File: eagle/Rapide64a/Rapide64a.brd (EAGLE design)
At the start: 50 x 50 mm, 25 parts, among them IC1 MEGA64-A, J1 AVR_SPI_PRG_6PTH

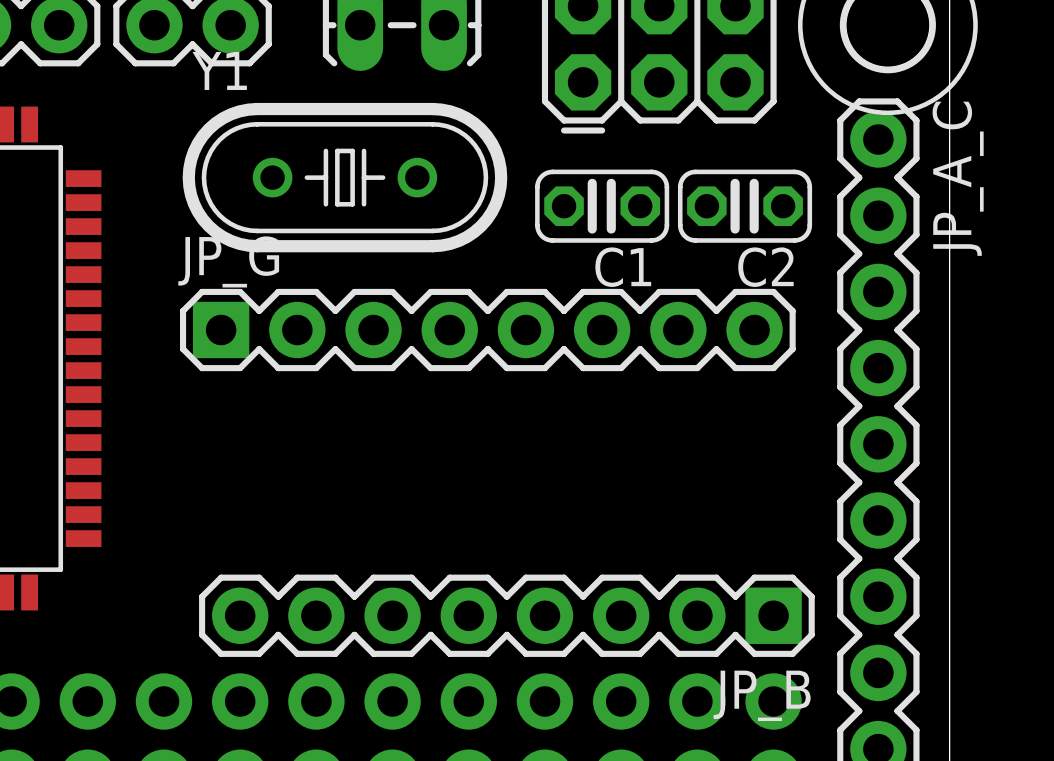
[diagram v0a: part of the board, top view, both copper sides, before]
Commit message: Added 2 pushbuttons
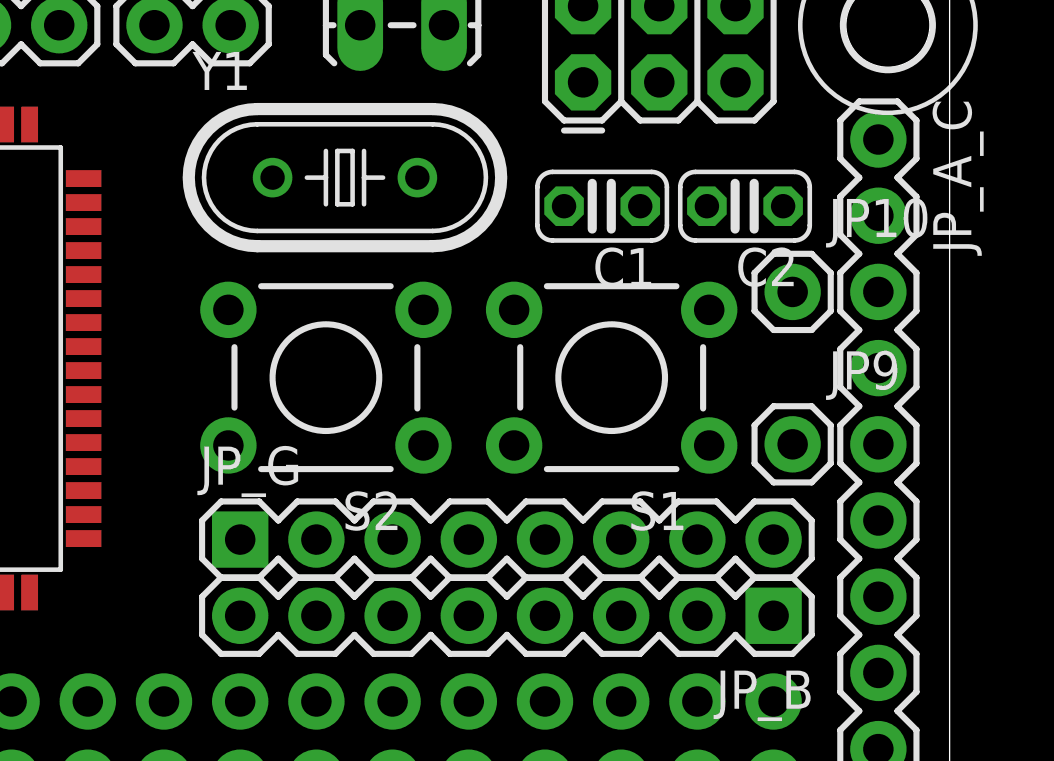
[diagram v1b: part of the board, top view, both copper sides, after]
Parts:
- added JP10, JP9: M01PTH, SparkFun-Connectors:1X01
- added S1, S2: SWITCH-MOMENTARY-2PTH, SparkFun-Electromechanical:TACTILE-PTH
- moved JP_G 7.01 mm to (26.4, 30.8)
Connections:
- new net N$55: JP9.1, S1.3
- new net N$56: JP10.1, S2.3
- net GND: now also S1.1, S2.1
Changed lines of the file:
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@@
 <element name="JP_B" library="SparkFun-Connectors" package="1X08" value="" x="44.1325" y="28.2575" rot="R180"/>
 <element name="JP_F" library="SparkFun-Connectors" package="1X08" value="" x="2.54" y="47.9425"/>
-<element name="JP_G" library="SparkFun-Connectors" package="1X08" value="" x="25.7175" y="37.7825"/>
+<element name="JP_G" library="SparkFun-Connectors" package="1X08" value="" x="26.3525" y="30.7975"/>
 <element name="JP_X" library="SparkFun-Connectors" package="1X02" value="" x="23.495" y="47.9425"/>
 <element name="C1" library="resistor" package="C025-024X044" value="22pF" x="38.4175" y="41.91" rot="R180"/>
@@
 <element name="H3" library="holes" package="2,8" value="MOUNT-HOLE2.8" x="47.9425" y="47.9425"/>
 <element name="JP8" library="SparkFun-Connectors" package="1X16_NO_SILK" value="M161X16_NO_SILK" x="6.0325" y="2.54"/>
+<element name="S1" library="SparkFun-Electromechanical" package="TACTILE-PTH" value="SWITCH-MOMENTARY-2PTH" x="38.735" y="36.195" rot="R180"/>
+<element name="S2" library="SparkFun-Electromechanical" package="TACTILE-PTH" value="SWITCH-MOMENTARY-2PTH" x="29.21" y="36.195" rot="R180"/>
+<element name="JP9" library="SparkFun-Connectors" package="1X01" value="M01PTH" x="44.7675" y="33.9725"/>
+<element name="JP10" library="SparkFun-Connectors" package="1X01" value="M01PTH" x="44.7675" y="39.0525"/>
 </elements>
 <signals>
@@
 <contactref element="J1" pad="3"/>
 <wire x1="41.5925" y1="28.2575" x2="40.3225" y2="46.0375" width="0" layer="19" extent="1-1"/>
-<wire x1="5.535" y1="34.83" x2="41.5925" y2="28.2575" width="0" layer="19" extent="1-1"/>
+<wire x1="5.535" y1="34.83" x2="40.3225" y2="46.0375" width="0" layer="19" extent="1-1"/>
 </signal>
 <signal name="N$35">
@@
 <contactref element="JP_G" pad="1"/>
 <contactref element="IC1" pad="1"/>
-<wire x1="5.535" y1="42.83" x2="25.7175" y2="37.7825" width="0" layer="19" extent="1-1"/>
+<wire x1="5.535" y1="42.83" x2="26.3525" y2="30.7975" width="0" layer="19" extent="1-1"/>
 </signal>
 <signal name="N$50">
 <contactref element="JP_G" pad="2"/>
 <contactref element="IC1" pad="33"/>
-<wire x1="21.135" y1="30.83" x2="28.2575" y2="37.7825" width="0" layer="19" extent="1-1"/>
+<wire x1="21.135" y1="30.83" x2="28.8925" y2="30.7975" width="0" layer="19" extent="1-1"/>
 </signal>
 <signal name="N$51">
 <contactref element="JP_G" pad="3"/>
 <contactref element="IC1" pad="34"/>
-<wire x1="21.135" y1="31.63" x2="30.7975" y2="37.7825" width="0" layer="19" extent="1-1"/>
+<wire x1="21.135" y1="31.63" x2="31.4325" y2="30.7975" width="0" layer="19" extent="1-1"/>
 </signal>
 <signal name="N$52">
 <contactref element="JP_G" pad="4"/>
 <contactref element="IC1" pad="43"/>
-<wire x1="21.135" y1="38.83" x2="33.3375" y2="37.7825" width="0" layer="19" extent="1-1"/>
+<wire x1="21.135" y1="38.83" x2="33.9725" y2="30.7975" width="0" layer="19" extent="1-1"/>
 </signal>
 <signal name="N$53">
 <contactref element="JP_G" pad="5"/>
 <contactref element="IC1" pad="19"/>
-<wire x1="8.935" y1="29.03" x2="35.8775" y2="37.7825" width="0" layer="19" extent="1-1"/>
+<wire x1="8.935" y1="29.03" x2="36.5125" y2="30.7975" width="0" layer="19" extent="1-1"/>
 </signal>
 <signal name="N$54">
 <contactref element="JP_G" pad="6"/>
 <contactref element="IC1" pad="18"/>
-<wire x1="8.135" y1="29.03" x2="38.4175" y2="37.7825" width="0" layer="19" extent="1-1"/>
+<wire x1="8.135" y1="29.03" x2="39.0525" y2="30.7975" width="0" layer="19" extent="1-1"/>
 </signal>
 <signal name="VCC">
@@
 <contactref element="JP_ROW_VCC" pad="16"/>
 <wire x1="33.147" y1="47.9425" x2="37.7825" y2="48.5775" width="0" layer="19" extent="1-1"/>
-<wire x1="43.4975" y1="37.7825" x2="37.7825" y2="48.5775" width="0" layer="19" extent="1-1"/>
 <wire x1="16.935" y1="44.63" x2="33.147" y2="47.9425" width="0" layer="19" extent="1-1"/>
 <wire x1="7.335" y1="44.63" x2="16.935" y2="44.63" width="0" layer="19" extent="1-1"/>
 <wire x1="10.535" y1="29.03" x2="7.335" y2="44.63" width="0" layer="19" extent="1-1"/>
+<wire x1="44.1325" y1="30.7975" x2="37.7825" y2="48.5775" width="0" layer="19" extent="1-1"/>
 <wire x1="11.1125" y1="10.16" x2="10.535" y2="29.03" width="0" layer="19" extent="1-1"/>
 <wire x1="13.6525" y1="10.16" x2="11.1125" y2="10.16" width="0" layer="19" extent="1-1"/>
@@
 <contactref element="JP_ROW_GND" pad="2"/>
 <contactref element="JP_ROW_GND" pad="1"/>
+<contactref element="S1" pad="1"/>
+<contactref element="S2" pad="1"/>
 <wire x1="44.45" y1="41.91" x2="42.8625" y2="48.5775" width="0" layer="19" extent="1-1"/>
-<wire x1="40.9575" y1="37.7825" x2="44.45" y2="41.91" width="0" layer="19" extent="1-1"/>
-<wire x1="39.6875" y1="41.91" x2="40.9575" y2="37.7825" width="0" layer="19" extent="1-1"/>
+<wire x1="39.6875" y1="41.91" x2="44.45" y2="41.91" width="0" layer="19" extent="1-1"/>
+<wire x1="41.9862" y1="33.9344" x2="39.6875" y2="41.91" width="0" layer="19" extent="1-1"/>
+<wire x1="41.5925" y1="30.7975" x2="41.9862" y2="33.9344" width="0" layer="19" extent="1-1"/>
+<wire x1="32.4612" y1="33.9344" x2="41.9862" y2="33.9344" width="0" layer="19" extent="1-1"/>
 <wire x1="30.353" y1="47.9425" x2="39.6875" y2="41.91" width="0" layer="19" extent="1-1"/>
 <wire x1="16.135" y1="44.63" x2="30.353" y2="47.9425" width="0" layer="19" extent="1-1"/>
 <wire x1="8.135" y1="44.63" x2="16.135" y2="44.63" width="0" layer="19" extent="1-1"/>
 <wire x1="11.335" y1="29.03" x2="8.135" y2="44.63" width="0" layer="19" extent="1-1"/>
-<wire x1="13.6525" y1="12.7" x2="11.335" y2="29.03" width="0" layer="19" extent="1-1"/>
+<wire x1="11.1125" y1="12.7" x2="11.335" y2="29.03" width="0" layer="19" extent="1-1"/>
+<wire x1="13.6525" y1="12.7" x2="11.1125" y2="12.7" width="0" layer="19" extent="1-1"/>
 <wire x1="16.1925" y1="12.7" x2="13.6525" y2="12.7" width="0" layer="19" extent="1-1"/>
 <wire x1="18.7325" y1="12.7" x2="16.1925" y2="12.7" width="0" layer="19" extent="1-1"/>
@@
 <wire x1="41.5925" y1="12.7" x2="39.0525" y2="12.7" width="0" layer="19" extent="1-1"/>
 <wire x1="44.1325" y1="12.7" x2="41.5925" y2="12.7" width="0" layer="19" extent="1-1"/>
-<wire x1="11.1125" y1="12.7" x2="13.6525" y2="12.7" width="0" layer="19" extent="1-1"/>
 <wire x1="8.5725" y1="12.7" x2="11.1125" y2="12.7" width="0" layer="19" extent="1-1"/>
 <wire x1="6.0325" y1="12.7" x2="8.5725" y2="12.7" width="0" layer="19" extent="1-1"/>
 </signal>
+<signal name="N$55">
+<contactref element="S1" pad="3"/>
+<contactref element="JP9" pad="1"/>
+<wire x1="44.7675" y1="33.9725" x2="41.9862" y2="38.4556" width="0" layer="19" extent="1-1"/>
+</signal>
+<signal name="N$56">
+<contactref element="S2" pad="3"/>
+<contactref element="JP10" pad="1"/>
+<wire x1="32.4612" y1="38.4556" x2="44.7675" y2="39.0525" width="0" layer="19" extent="1-1"/>
+</signal>
 </signals>

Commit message: Work in progress, 40% wiring done.
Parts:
- JP_POWER: device SparkFun-Connectors:1X02_LOCK_LONGPADS -> SparkFun-Connectors:1X02
- moved JP_B 17.8 mm to (26.4, 28.3), turned to 0 degrees
- moved JP_F 0.71 mm to (1.91, 48.3)
- moved JP_X 0.71 mm to (24.1, 48.3)
- moved J1 0.32 mm to (37.8, 45.7)
- moved Y1 0.32 mm to (30.2, 42.9), turned to 180 degrees
- moved JP_G 0.32 mm to (26.4, 31.1)
- moved C1 0.32 mm to (38.4, 41.6)
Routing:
- net GND: track 0.00 -> 160.1 mm, vias 0 -> 2
- net VCC: track 0.00 -> 129.0 mm, vias 0 -> 2
- net N$68: track 0.00 -> 53.1 mm
- net N$17: track 0.00 -> 50.7 mm, vias 0 -> 1
- net N$35: track 0.00 -> 47.5 mm
- net N$67: track 0.00 -> 47.0 mm
- net N$44: track 0.00 -> 46.2 mm, vias 0 -> 1
- net N$36: track 0.00 -> 42.2 mm
- net N$66: track 0.00 -> 40.4 mm
- net N$43: track 0.00 -> 39.9 mm, vias 0 -> 1
- net N$65: track 0.00 -> 34.3 mm
- net N$58: track 0.00 -> 27.5 mm, vias 0 -> 1
- net N$64: track 0.00 -> 27.1 mm
- net N$8: track 0.00 -> 22.1 mm
- net N$6: track 0.00 -> 21.4 mm, vias 0 -> 1
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
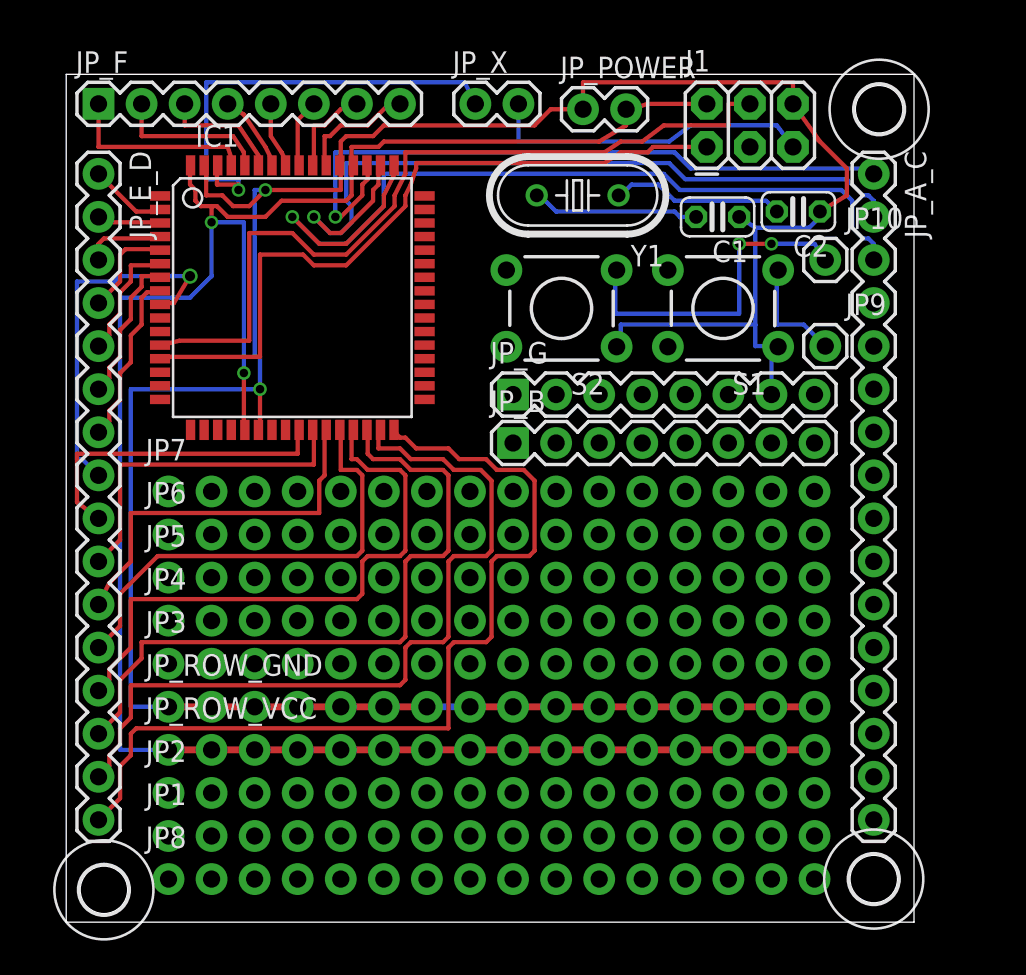
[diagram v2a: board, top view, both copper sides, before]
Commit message: Work in progress, changed layout a little, 60% wiring
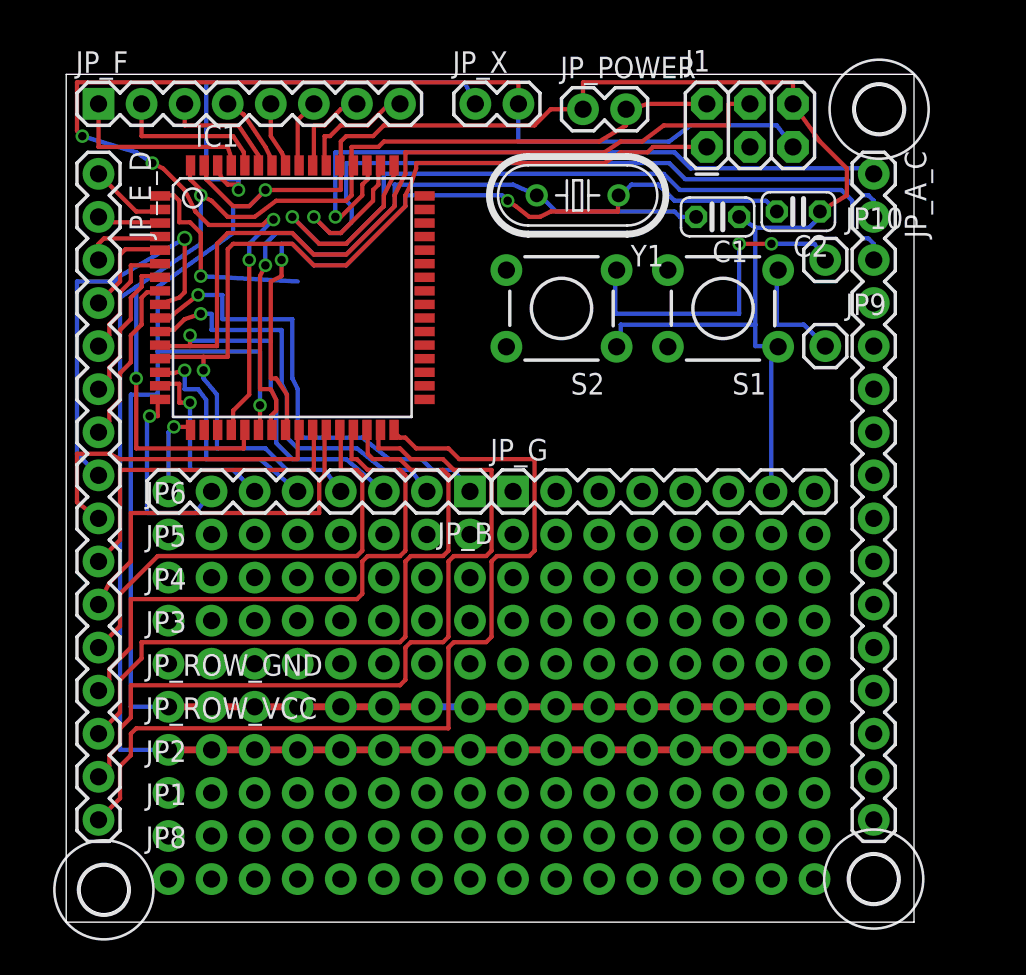
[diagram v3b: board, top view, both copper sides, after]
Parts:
- removed JP7: M161X16_NO_SILK, SparkFun-Connectors:1X16_NO_SILK
- moved JP_G 5.71 mm to (26.4, 25.4)
- moved JP_B 3.82 mm to (23.8, 25.4), turned to 180 degrees
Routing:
- net N$57: track 19.4 -> 77.0 mm, vias 0 -> 4
- net N$80: track 0.00 -> 36.1 mm, vias 0 -> 2
- net N$59: track 9.73 -> 41.0 mm, vias 0 -> 1
- net N$16: track 0.00 -> 28.3 mm, vias 0 -> 1
- net N$15: track 0.00 -> 24.6 mm, vias 0 -> 1
- net N$35: track 47.5 -> 66.7 mm, vias 0 -> 1
- net N$36: track 42.2 -> 57.0 mm, vias 0 -> 1
- net N$42: track 0.00 -> 13.9 mm, vias 0 -> 1
- net N$19: track 0.00 -> 12.2 mm, vias 0 -> 1
- net N$48: track 0.00 -> 11.6 mm, vias 0 -> 1
- net N$45: track 0.00 -> 11.3 mm, vias 0 -> 1
- net GND: track 160.1 -> 170.1 mm
- net N$18: track 0.00 -> 5.21 mm, vias 0 -> 1
- net N$6: track 21.4 -> 23.7 mm
- net VCC: track 129.0 -> 130.2 mm
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
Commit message: Wiring finished, must be validated and improved now.
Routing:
- net N$49: track 0.00 -> 64.2 mm, vias 0 -> 1
- net N$50: track 0.00 -> 59.3 mm, vias 0 -> 1
- net N$37: track 0.00 -> 56.7 mm, vias 0 -> 2
- net N$51: track 0.00 -> 54.6 mm, vias 0 -> 1
- net N$24: track 0.00 -> 49.0 mm, vias 0 -> 1
- net N$69: track 0.00 -> 48.3 mm, vias 0 -> 1
- net N$22: track 0.00 -> 48.0 mm, vias 0 -> 2
- net N$73: track 0.00 -> 46.9 mm, vias 0 -> 1
- net N$23: track 0.00 -> 43.9 mm, vias 0 -> 2
- net VCC: track 130.2 -> 173.4 mm
- net N$47: track 0.00 -> 40.6 mm, vias 0 -> 2
- net N$75: track 0.00 -> 37.4 mm, vias 0 -> 3
- net N$15: track 24.6 -> 61.6 mm, vias 1 -> 4
- net N$40: track 0.00 -> 37.0 mm
- net N$56: track 0.00 -> 35.1 mm
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
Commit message: Should be ok, added anotations, logos,... Check tomorrow if ready for production and go.
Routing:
- net VCC: track 173.4 -> 199.7 mm
- net GND: track 170.3 -> 168.3 mm, vias 2 -> 3
- added copper zone on layer 16, net GND
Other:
- board text added: "+"
- board text added: "-"
- board text added: "A"
- board text added: "ATmega64a"
- board text added: "B"
- board text added: "C"
- board text added: "D"
- board text added: "Dec2012 v1.0"
- board text added: "E"
- board text added: "F"
- board text added: "G"
- board text added: "REF"
- board text added: "RST"
- board text added: "Rapide64a"
- board text added: "X"
- board text added: "Z"
- board text added: "http://kalshagar.wikispaces.com/Rapide64a"
